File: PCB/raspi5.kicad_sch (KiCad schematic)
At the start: 6 parts, among them J1 GPIO, J3 68711614522, U1 BL24C256A

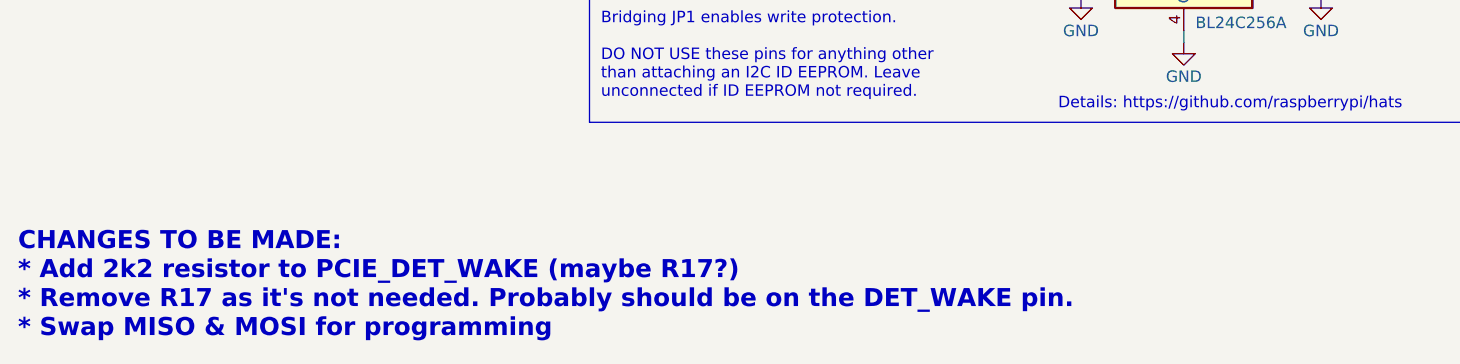
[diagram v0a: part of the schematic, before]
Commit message: Updated PCB to remove MOSI-MISO cross. Updated texts. New images.
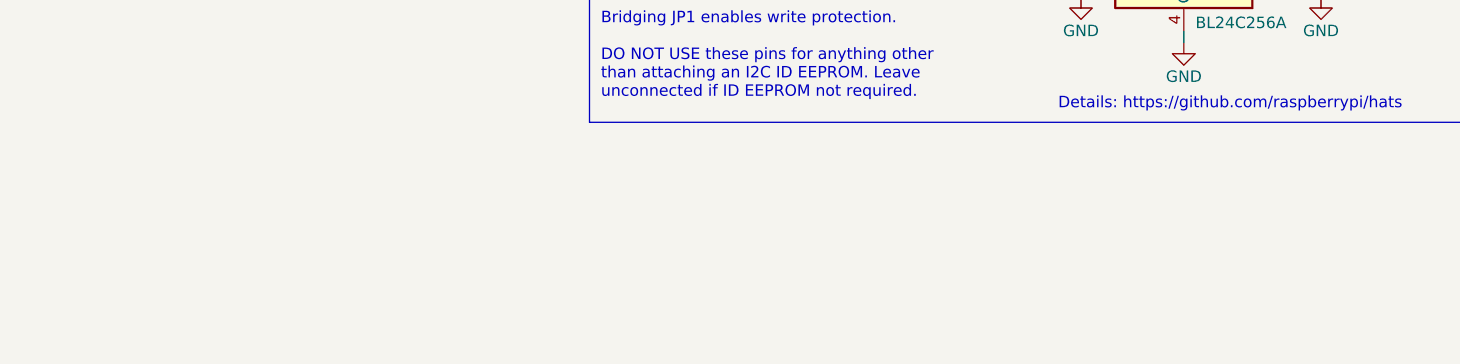
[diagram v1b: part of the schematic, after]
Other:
- note removed: "CHANGES TO BE MADE: * Add 2k2 resistor to PCIE_DET_WAKE (maybe R17?) * Remove R17 as it's not needed. Probably should be on the DET_WAKE pin. * Swap MISO & MOSI for programming"
